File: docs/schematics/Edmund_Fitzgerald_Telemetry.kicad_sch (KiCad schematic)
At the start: 5 parts, among them Q1 MOSFET_N, U1 ESP32_Control

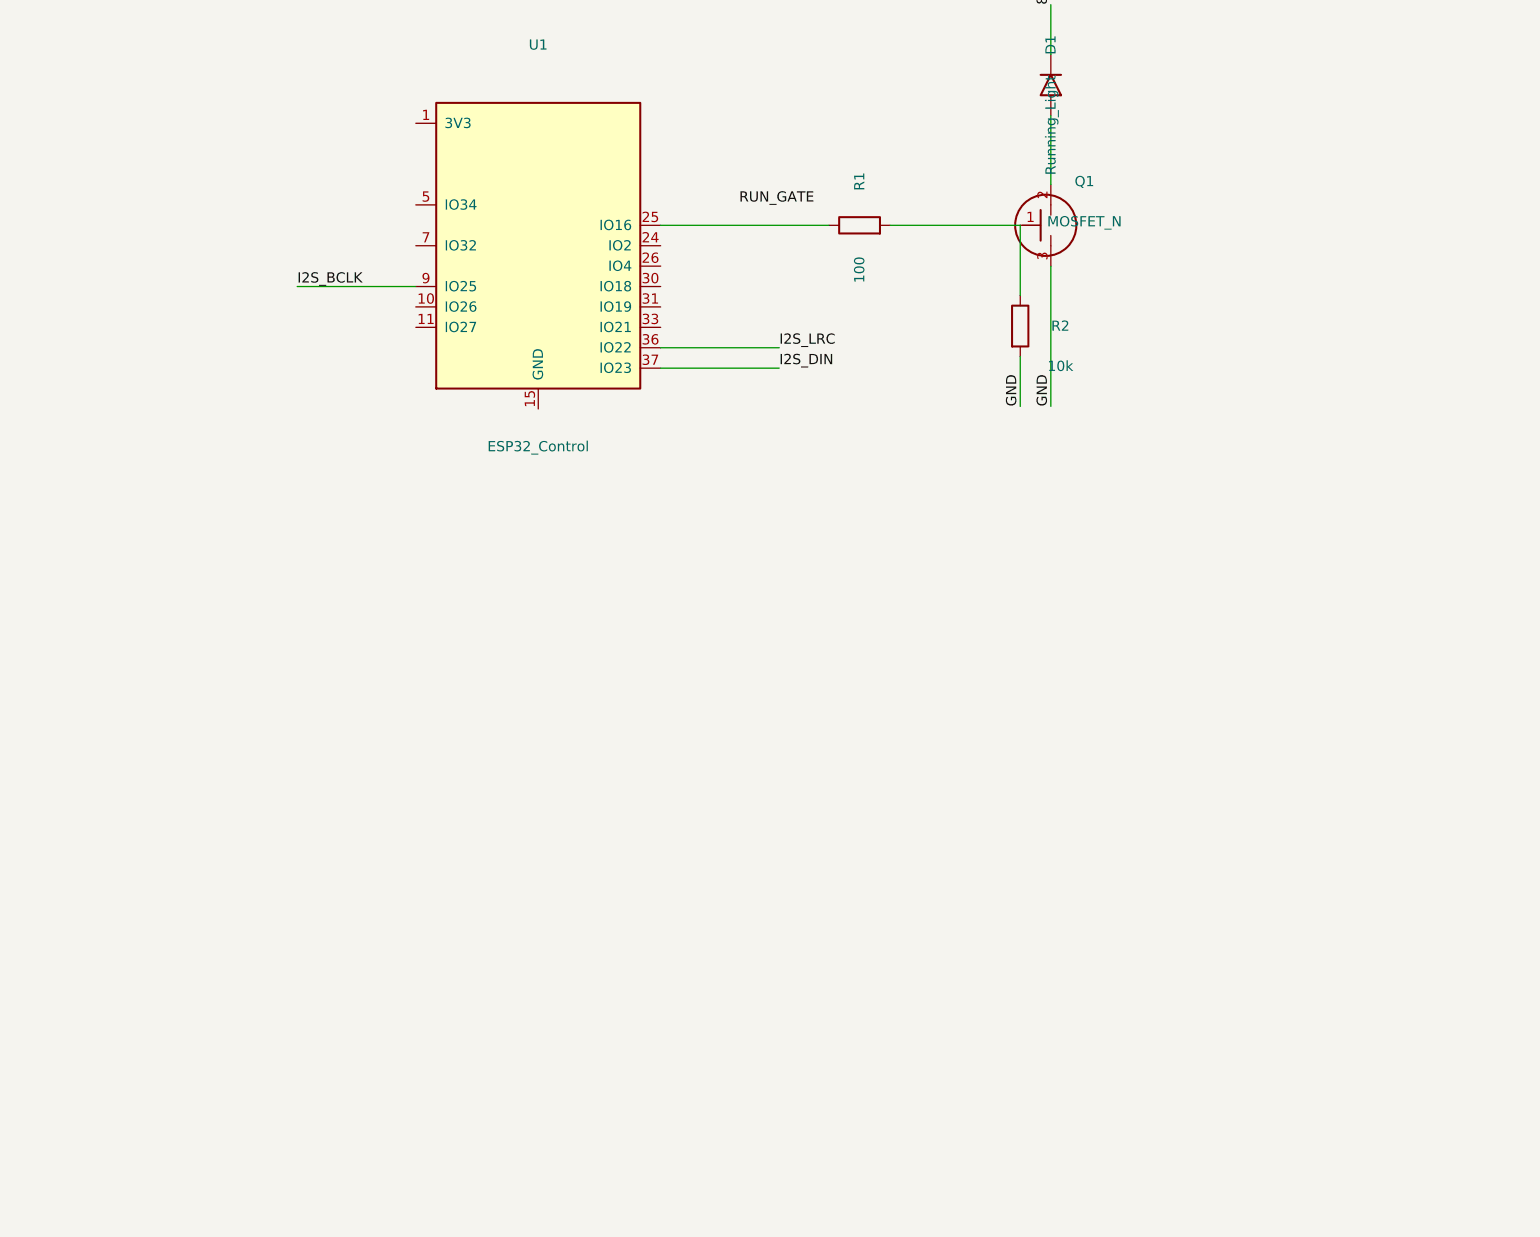
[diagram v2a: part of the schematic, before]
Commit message: Consolidate full schematic circuit into v2.0 stable state
- Restored ESP32, MOSFETs, Battery Sense, and Water Sensor
- Included fixed Audio Modules (MAX98357A and DFPlayer Pro)
- Cleaned up layout to prevent overlapping components
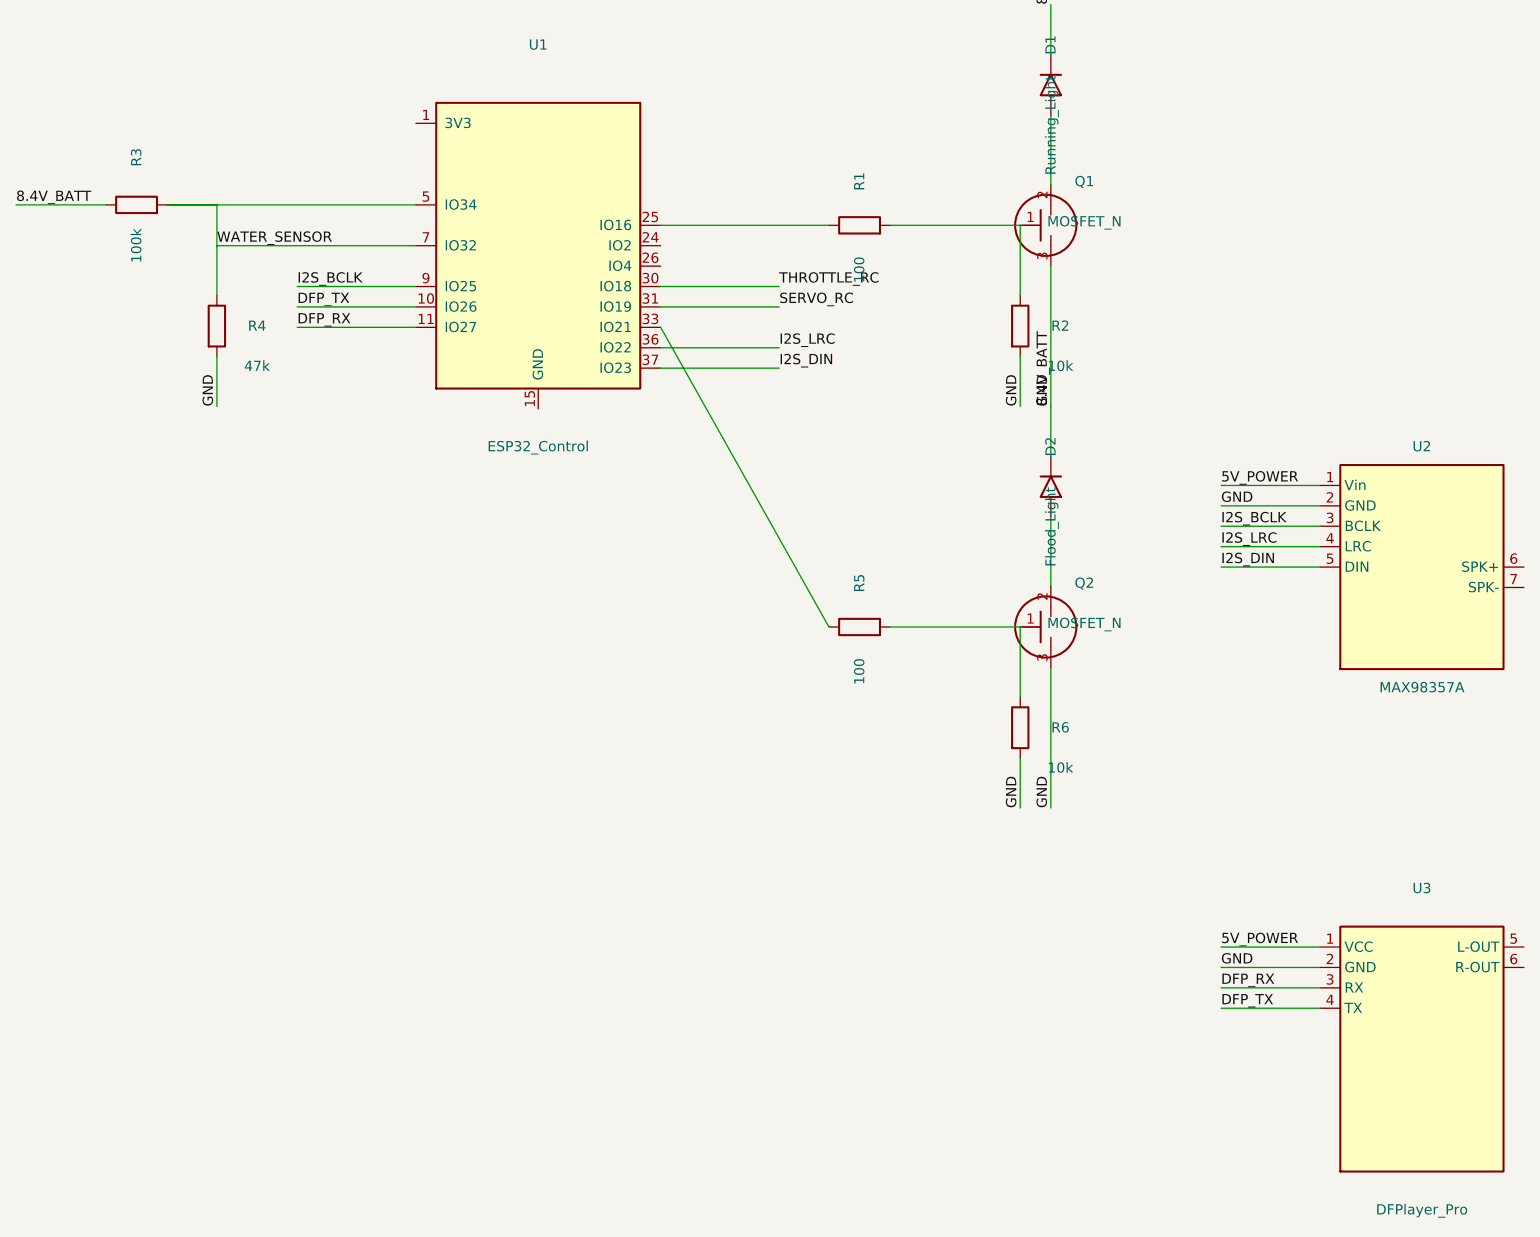
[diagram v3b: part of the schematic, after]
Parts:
- added D2: Flood_Light, symbol Device:LED
- added Q2: MOSFET_N, symbol Transistor_FET:Q_NMOS_GDS
- added R3: 100k, symbol Device:R
- added R4: 47k, symbol Device:R
- added R5: 100, symbol Device:R
- added R6: 10k, symbol Device:R
- added U2: MAX98357A, symbol Module:MAX98357A
- added U3: DFPlayer_Pro, symbol Module:DFPlayer_Pro
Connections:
- net GND is gone; now on net 8.4V_BATT: Q1.3 (S), R2.2
- net 8.4V_BATT: now also D2.2 (A), Q2.3 (S), R3.1, R4.2, R6.2, U2.2 (GND), U3.2 (GND)
- net I2S_BCLK: now also U2.3 (BCLK)
- net I2S_DIN: now also U2.5 (DIN)
- net I2S_LRC: now also U2.4 (LRC)
- net DFP_TX: now reaches U1.10 (IO26)
- net DFP_TX: now also U3.4 (TX)
- net DFP_RX: now reaches U1.11 (IO27)
- net DFP_RX: now also U3.3 (RX)
- net THROTTLE_RC: now reaches U1.30 (IO18)
- net SERVO_RC: now reaches U1.31 (IO19)
- net at U1.33 (IO21): now also R5.1
- net WATER_SENSOR: now reaches U1.5 (IO34)
- net WATER_SENSOR: now also U1.7 (IO32), R3.2, R4.1
- new net: Q2.1 (G), R5.2, R6.1
- new net: D2.1 (K), Q2.2 (D)
- new net 5V_POWER: U2.1 (Vin), U3.1 (VCC)
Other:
- title: Edmund Fitzgerald - Platform Telemetry -> Edmund Fitzgerald - FULL SYSTEM
